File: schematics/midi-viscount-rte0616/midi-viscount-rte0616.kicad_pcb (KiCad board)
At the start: 2 copper layers, 8 parts, among them J1 Conn_02x07_Odd_Even, U1 ProMicro

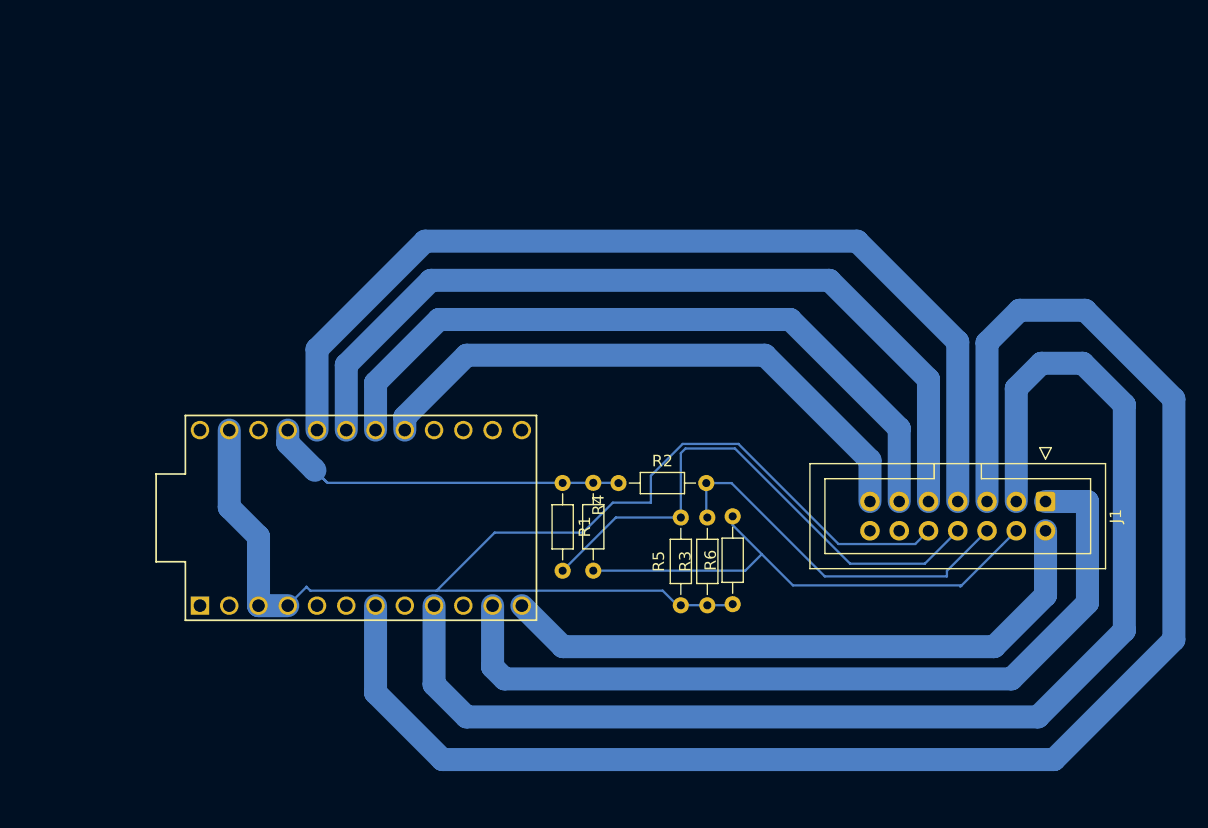
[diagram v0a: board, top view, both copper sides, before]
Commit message: Use potentiometers instead of resistors
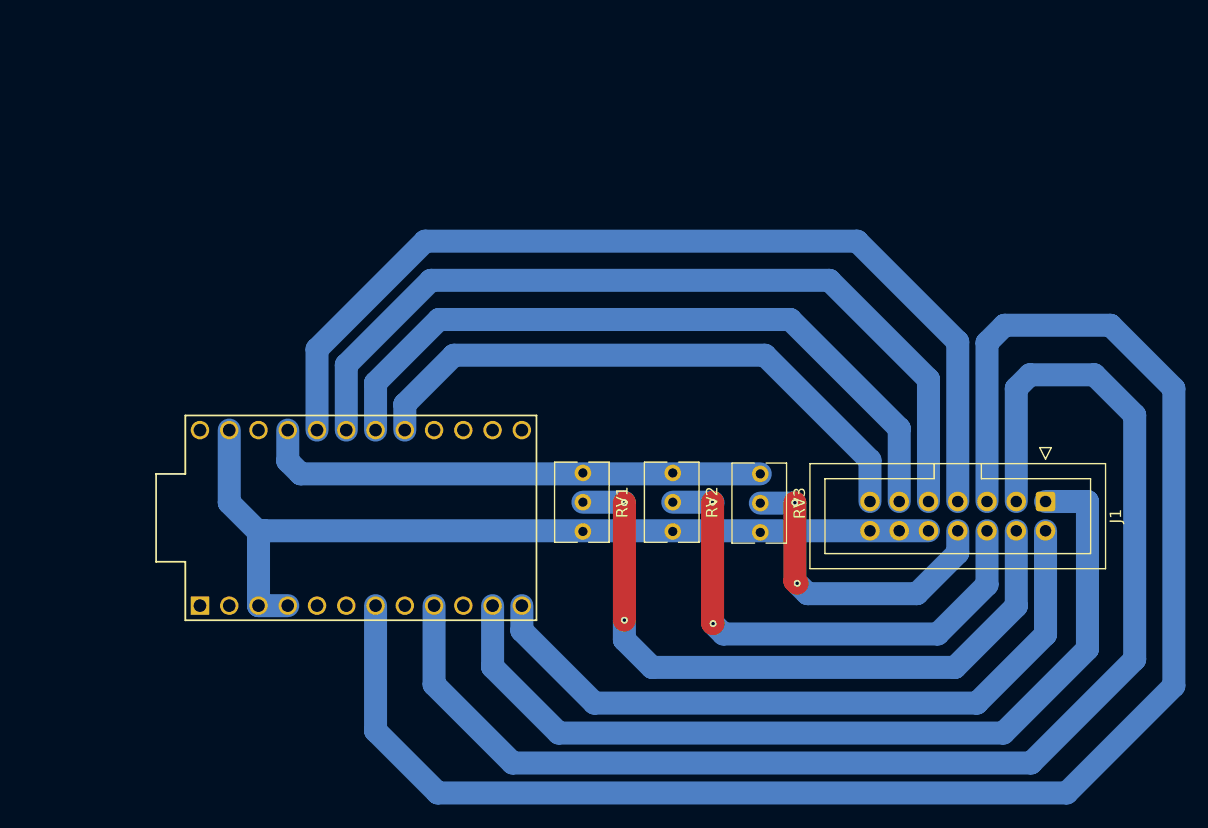
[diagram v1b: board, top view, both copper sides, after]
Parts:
- removed R1, R2, R3, R4: 220, Resistor_THT:R_Axial_DIN0204_L3.6mm_D1.6mm_P7.62mm_Horizontal
- removed R5: 100, Resistor_THT:R_Axial_DIN0204_L3.6mm_D1.6mm_P7.62mm_Horizontal
- removed R6: 1k, Resistor_THT:R_Axial_DIN0204_L3.6mm_D1.6mm_P7.62mm_Horizontal
- added RV1: R_Potentiometer, Potentiometer_THT:Potentiometer_Bourns_3266Y_Vertical, F.Cu at (77.9, 65.9)
- added RV2: R_Potentiometer, Potentiometer_THT:Potentiometer_Bourns_3266Y_Vertical, F.Cu at (85.7, 65.9)
- added RV3: R_Potentiometer, Potentiometer_THT:Potentiometer_Bourns_3266Y_Vertical, F.Cu at (93.3, 66.0)
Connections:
- J1 pad 10: GND -> Vseg4
- J1 pad 12: unconnected-(J1-Pin_12-Pad12) -> Vseg4
- J1 pad 14: unconnected-(J1-Pin_14-Pad14) -> Vseg4
- J1 pad 4: Net-(J1-Pin_4) -> Vseg1
- J1 pad 6: Net-(J1-Pin_6) -> Vseg2
- J1 pad 8: Net-(J1-Pin_8) -> VSeg3
- U1 pad 23: GND -> Vseg4
- U1 pad 3: GND -> Vseg4
- U1 pad 4: GND -> Vseg4
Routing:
- net GND: track 112.1 -> 0.00 mm
- net Vseg4: track 0.00 -> 77.2 mm
- net Vseg1: track 0.00 -> 59.3 mm, vias 0 -> 2
- net Net-(J1-Pin_8): track 47.3 -> 0.00 mm
- net Net-(J1-Pin_4): track 45.4 -> 0.00 mm
- net Vseg2: track 0.00 -> 44.7 mm, vias 0 -> 2
- net Net-(J1-Pin_6): track 32.7 -> 0.00 mm
- net VSeg3: track 0.00 -> 27.8 mm, vias 0 -> 2
- net Net-(U1-VCC): track 33.1 -> 44.2 mm
- net Net-(J1-Pin_2): track 54.4 -> 61.7 mm
- net Net-(J1-Pin_1): track 72.6 -> 78.8 mm
- net Net-(J1-Pin_5): track 138.8 -> 145.0 mm
- net Net-(J1-Pin_3): track 112.2 -> 117.5 mm
- net Net-(J1-Pin_13): track 51.1 -> 51.7 mm

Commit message: Add pin headers for pedals
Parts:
- added J10: Conn_01x01_Pin, Connector_PinHeader_2.54mm:PinHeader_1x01_P2.54mm_Vertical, F.Cu at (54.8, 77.8)
- added J11: Conn_01x01_Pin, Connector_PinHeader_2.54mm:PinHeader_1x01_P2.54mm_Vertical, F.Cu at (54.8, 82.4)
- added J12: Conn_01x01_Pin, Connector_PinHeader_2.54mm:PinHeader_1x01_P2.54mm_Vertical, F.Cu at (51.2, 77.8)
- added J13: Conn_01x01_Pin, Connector_PinHeader_2.54mm:PinHeader_1x01_P2.54mm_Vertical, F.Cu at (51.2, 82.4)
- added J2: Conn_01x01_Pin, Connector_PinHeader_2.54mm:PinHeader_1x01_P2.54mm_Vertical, F.Cu at (81.0, 51.1)
- added J3: Conn_01x01_Pin, Connector_PinHeader_2.54mm:PinHeader_1x01_P2.54mm_Vertical, F.Cu at (85.6, 51.1)
- added J4: Conn_01x01_Pin, Connector_PinHeader_2.54mm:PinHeader_1x01_P2.54mm_Vertical, F.Cu at (90.3, 51.2)
- added J5: Conn_01x01_Pin, Connector_PinHeader_2.54mm:PinHeader_1x01_P2.54mm_Vertical, F.Cu at (94.9, 51.2)
- added J6: Conn_01x01_Pin, Connector_PinHeader_2.54mm:PinHeader_1x01_P2.54mm_Vertical, F.Cu at (81.0, 55.8)
- added J7: Conn_01x01_Pin, Connector_PinHeader_2.54mm:PinHeader_1x01_P2.54mm_Vertical, F.Cu at (85.6, 55.8)
- added J8: Conn_01x01_Pin, Connector_PinHeader_2.54mm:PinHeader_1x01_P2.54mm_Vertical, F.Cu at (90.3, 55.8)
- added J9: Conn_01x01_Pin, Connector_PinHeader_2.54mm:PinHeader_1x01_P2.54mm_Vertical, F.Cu at (94.9, 55.8)
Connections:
- U1 pad 13: unconnected-(U1-B6-Pad13) -> Net-(J2-Pin_1)
- U1 pad 14: unconnected-(U1-B2-Pad14) -> Net-(J3-Pin_1)
- U1 pad 15: unconnected-(U1-B3-Pad15) -> Net-(J4-Pin_1)
- U1 pad 16: unconnected-(U1-B1-Pad16) -> Net-(J5-Pin_1)
- U1 pad 5: unconnected-(U1-SDA-Pad5) -> Net-(J10-Pin_1)
- U1 pad 6: unconnected-(U1-SCL-Pad6) -> Net-(J11-Pin_1)
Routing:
- net Net-(J5-Pin_1): track 0.00 -> 44.2 mm
- net Vseg4: track 77.2 -> 115.6 mm
- net Net-(J4-Pin_1): track 0.00 -> 33.9 mm
- net Net-(J3-Pin_1): track 0.00 -> 22.7 mm
- net Net-(J1-Pin_13): track 51.7 -> 68.9 mm
- net Net-(J1-Pin_11): track 62.1 -> 79.2 mm
- net Net-(J1-Pin_9): track 73.4 -> 88.4 mm
- net Net-(J1-Pin_7): track 84.0 -> 98.1 mm
- net Net-(J1-Pin_5): track 145.0 -> 132.3 mm
- net Net-(J11-Pin_1): track 0.00 -> 11.1 mm
- net Net-(J2-Pin_1): track 0.00 -> 10.8 mm
- net Net-(J1-Pin_3): track 117.5 -> 107.8 mm
- net Net-(J10-Pin_1): track 0.00 -> 5.47 mm

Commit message: Schematics rev1.1
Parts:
- added REF**: MountingHole_2.2mm_M2_ISO7380, MountingHole:MountingHole_2.2mm_M2_ISO7380, F.Cu at (51.5, 62.7)
- added REF**: MountingHole_2.2mm_M2_ISO7380, MountingHole:MountingHole_2.2mm_M2_ISO7380, F.Cu at (108.9, 77.7)
- added REF**: MountingHole_2.2mm_M2_ISO7380, MountingHole:MountingHole_2.2mm_M2_ISO7380, F.Cu at (44.9, 28.7)
- added REF**: MountingHole_2.2mm_M2_ISO7380, MountingHole:MountingHole_2.2mm_M2_ISO7380, F.Cu at (108.9, 28.7)
- moved J1 60.6 mm to (62.5, 39.2)
- moved J13 46.6 mm to (92.8, 61.4), turned to -90 degrees
- moved J12 41.8 mm to (92.8, 65.0), turned to -90 degrees
- moved J11 40.3 mm to (88.0, 61.4), turned to -90 degrees
- moved RV1 39.8 mm to (107.5, 39.3), turned to 90 degrees
- moved J10 35.6 mm to (88.0, 65.0), turned to -90 degrees
- moved RV2 30.1 mm to (99.7, 39.3), turned to 90 degrees
- moved J9 29.1 mm to (71.0, 39.2), turned to 180 degrees
- moved RV3 26.8 mm to (92.1, 39.2), turned to 90 degrees
- moved J8 25.1 mm to (71.0, 43.8), turned to 180 degrees
- moved J7 22.1 mm to (75.7, 39.2), turned to 180 degrees
- moved J5 17.4 mm to (80.3, 39.2), turned to 180 degrees
- moved J3 17.1 mm to (85.0, 39.2), turned to 180 degrees
- moved J6 16.4 mm to (75.7, 43.8), turned to 180 degrees
- moved J4 8.94 mm to (80.3, 43.9), turned to 180 degrees
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- renumbered J12 to J11, J11 to J12, J6 to J3, J3 to J4, J7 to J5, J4 to J6, J8 to J7, J5 to J8
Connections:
- J1 pad 1: Net-(J1-Pin_1) -> Vseg4
- J1 pad 10: Vseg4 -> Net-(J1-Pin_10)
- J1 pad 11: Net-(J1-Pin_11) -> Vseg1
- J1 pad 12: Vseg4 -> Net-(J1-Pin_12)
- J1 pad 14: Vseg4 -> Net-(J1-Pin_14)
- J1 pad 3: Net-(J1-Pin_3) -> Vseg4
- J1 pad 4: Vseg1 -> Net-(J1-Pin_4)
- J1 pad 5: Net-(J1-Pin_5) -> Vseg4
- J1 pad 6: Vseg2 -> Net-(J1-Pin_6)
- J1 pad 7: Net-(J1-Pin_7) -> VSeg3
- J1 pad 8: VSeg3 -> Net-(J1-Pin_8)
- J1 pad 9: Net-(J1-Pin_9) -> Vseg2
- U1 pad 11: Net-(J1-Pin_1) -> Net-(J1-Pin_14)
- U1 pad 12: Net-(J1-Pin_2) -> Net-(J1-Pin_13)
- U1 pad 17: Net-(J1-Pin_13) -> Net-(J1-Pin_2)
- U1 pad 18: Net-(J1-Pin_11) -> Net-(J1-Pin_4)
- U1 pad 19: Net-(J1-Pin_9) -> Net-(J1-Pin_6)
- U1 pad 20: Net-(J1-Pin_7) -> Net-(J1-Pin_8)
- U1 pad 7: Net-(J1-Pin_5) -> Net-(J1-Pin_10)
- U1 pad 9: Net-(J1-Pin_3) -> Net-(J1-Pin_12)
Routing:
- net Net-(J1-Pin_5): track 132.3 -> 0.00 mm
- net Net-(J1-Pin_3): track 107.8 -> 0.00 mm
- net Net-(J1-Pin_7): track 98.1 -> 0.00 mm
- net Net-(J1-Pin_9): track 88.4 -> 0.00 mm
- net Net-(J1-Pin_11): track 79.2 -> 0.00 mm
- net Net-(J1-Pin_1): track 78.8 -> 0.00 mm
- net Net-(J1-Pin_14): track 0.00 -> 74.7 mm
- net Net-(J1-Pin_13): track 68.9 -> 135.3 mm
- net Net-(J1-Pin_12): track 0.00 -> 64.0 mm
- net Net-(J1-Pin_10): track 0.00 -> 52.9 mm
- net Net-(J1-Pin_2): track 61.7 -> 15.5 mm
- net Net-(U1-VCC): track 44.2 -> 78.7 mm
- net Net-(J8-Pin_1): track 44.2 -> 11.5 mm
- net Net-(J10-Pin_1): track 5.47 -> 31.7 mm
- net Net-(J12-Pin_1): track 11.1 -> 33.0 mm
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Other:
- board outline added: 72.1 x 56.5 mm
- board text added: "github.com/gwilherm/midi-viscount-rte0616"
- board text added: "rev1.1"
